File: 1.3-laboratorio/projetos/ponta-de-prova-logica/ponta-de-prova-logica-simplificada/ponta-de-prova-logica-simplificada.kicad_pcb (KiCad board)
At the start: 2 copper layers, 18 parts, among them J1 TEST PROBE, J2 Conn_01x02, U1 LM319

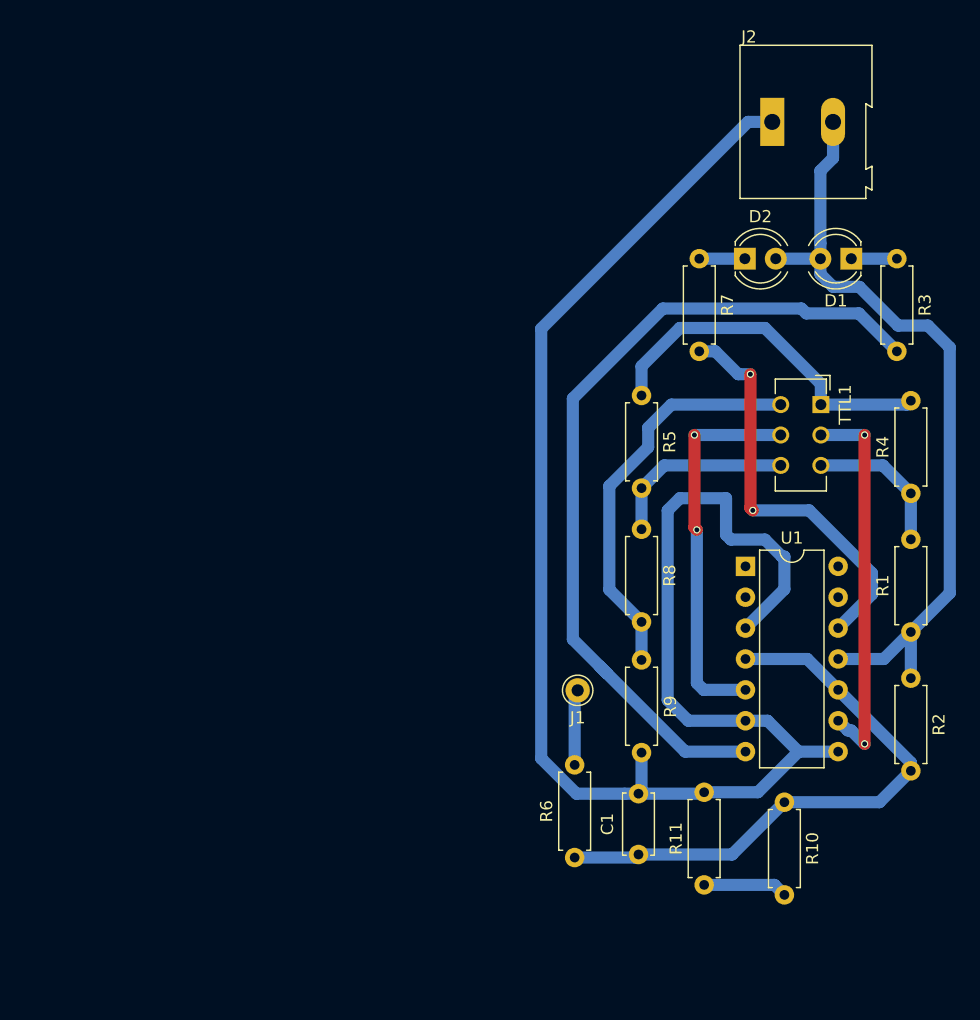
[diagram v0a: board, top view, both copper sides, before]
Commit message: Nova versão da Ponta de Prova Lógica - PCI em elaboração.
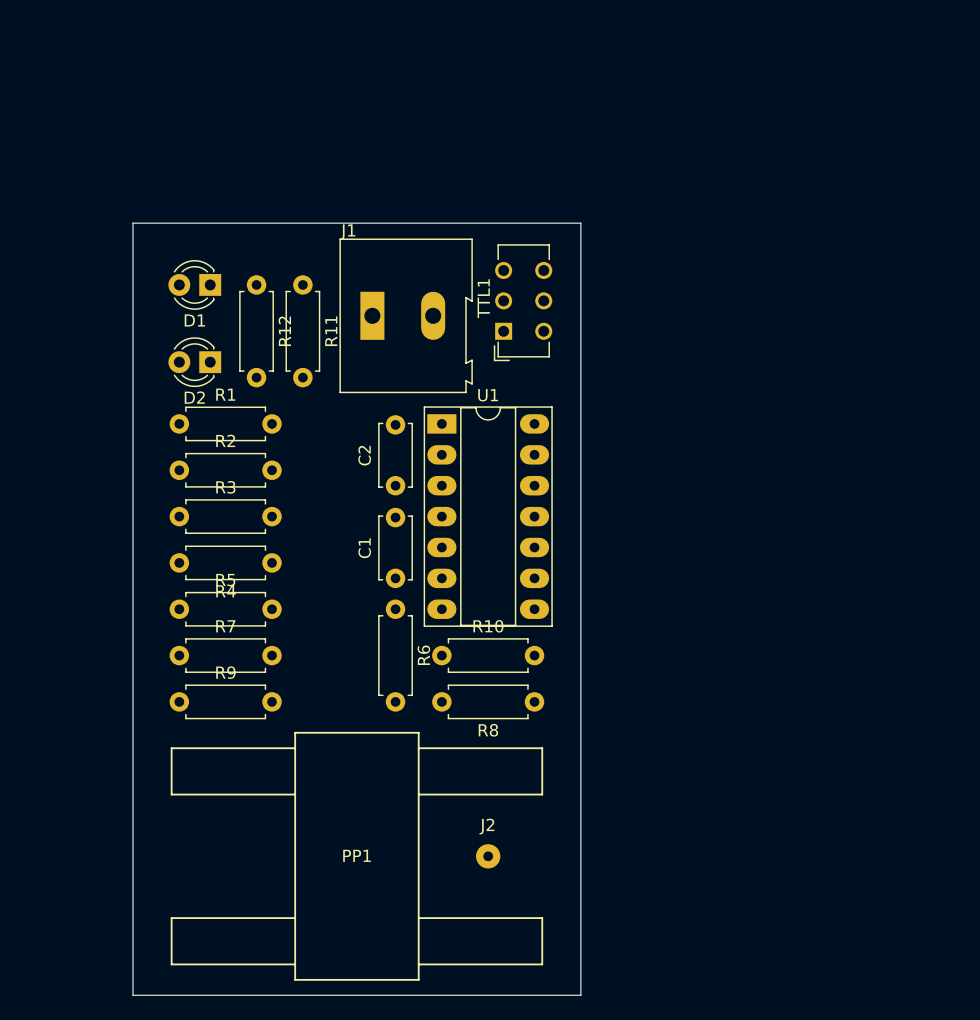
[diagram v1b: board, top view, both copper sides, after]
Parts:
- added C2: 100nF, Capacitor_THT:C_Disc_D5.0mm_W2.5mm_P5.00mm, F.Cu at (160.0, 90.2)
- added PP1: ponta-de-prova-fixacao-20mm-x-10mm-x-10mm, ponta-de-prova-fixacao-20mm-x-10mm-x-10mm, F.Cu at (151.8, 110.5)
- added R12: 820/0.5W, Resistor_THT:R_Axial_DIN0207_L6.3mm_D2.5mm_P7.62mm_Horizontal, F.Cu at (148.6, 73.7)
- C1: footprint Capacitors_THT:C_Disc_D5.0mm_W2.5mm_P5.00mm -> Capacitor_THT:C_Disc_D5.0mm_W2.5mm_P5.00mm
- D1: value LED HIGH -> LED ALTO; footprint LEDs:LED_D4.0mm -> LED_THT:LED_D3.0mm
- D2: value LED LOW -> LED BAIXO; footprint LEDs:LED_D4.0mm -> LED_THT:LED_D3.0mm
- J1: value TEST PROBE -> Conn_01x02; footprint Connectors:Pin_d1.0mm_L10.0mm -> TerminalBlock:TerminalBlock_Altech_AK300-2_P5.00mm
- J2: value Conn_01x02 -> PONTA DE PROVA; footprint Connectors_Terminal_Blocks:TerminalBlock_Altech_AK300-2_P5.00mm -> Connector_Wire:SolderWirePad_1x01_Drill0.8mm
- R1, R6: footprint Resistors_THT:R_Axial_DIN0207_L6.3mm_D2.5mm_P7.62mm_Horizontal -> Resistor_THT:R_Axial_DIN0207_L6.3mm_D2.5mm_P7.62mm_Horizontal
- R10: value 680k -> 10M; footprint Resistors_THT:R_Axial_DIN0207_L6.3mm_D2.5mm_P7.62mm_Horizontal -> Resistor_THT:R_Axial_DIN0207_L6.3mm_D2.5mm_P7.62mm_Horizontal
- R11: value 390k -> 820/0.5W; footprint Resistors_THT:R_Axial_DIN0207_L6.3mm_D2.5mm_P7.62mm_Horizontal -> Resistor_THT:R_Axial_DIN0207_L6.3mm_D2.5mm_P7.62mm_Horizontal
- R2: value 1.2M -> 56k; footprint Resistors_THT:R_Axial_DIN0207_L6.3mm_D2.5mm_P7.62mm_Horizontal -> Resistor_THT:R_Axial_DIN0207_L6.3mm_D2.5mm_P7.62mm_Horizontal
- R3: value 560/0.5W -> 22k; footprint Resistors_THT:R_Axial_DIN0207_L6.3mm_D2.5mm_P7.62mm_Horizontal -> Resistor_THT:R_Axial_DIN0207_L6.3mm_D2.5mm_P7.62mm_Horizontal
- R4: value 56k -> 47k; footprint Resistors_THT:R_Axial_DIN0207_L6.3mm_D2.5mm_P7.62mm_Horizontal -> Resistor_THT:R_Axial_DIN0207_L6.3mm_D2.5mm_P7.62mm_Horizontal
- R5: value 22k -> 33k; footprint Resistors_THT:R_Axial_DIN0207_L6.3mm_D2.5mm_P7.62mm_Horizontal -> Resistor_THT:R_Axial_DIN0207_L6.3mm_D2.5mm_P7.62mm_Horizontal
- R7: value 560/0.5W -> 1.2M; footprint Resistors_THT:R_Axial_DIN0207_L6.3mm_D2.5mm_P7.62mm_Horizontal -> Resistor_THT:R_Axial_DIN0207_L6.3mm_D2.5mm_P7.62mm_Horizontal
- R8: value 47k -> 680k; footprint Resistors_THT:R_Axial_DIN0207_L6.3mm_D2.5mm_P7.62mm_Horizontal -> Resistor_THT:R_Axial_DIN0207_L6.3mm_D2.5mm_P7.62mm_Horizontal
- R9: value 33k -> 390k; footprint Resistors_THT:R_Axial_DIN0207_L6.3mm_D2.5mm_P7.62mm_Horizontal -> Resistor_THT:R_Axial_DIN0207_L6.3mm_D2.5mm_P7.62mm_Horizontal
- TTL1: footprint Buttons_Switches_THT:SW_CuK_JS202011AQN_DPDT_Angled -> Button_Switch_THT:SW_CuK_JS202011CQN_DPDT_Straight
- U1: value LM319 -> LM339; footprint Housings_DIP:DIP-14_W7.62mm -> Package_DIP:DIP-14_W7.62mm_Socket_LongPads
- moved J2 64.8 mm to (167.6, 120.7)
- moved R3 62.7 mm to (142.2, 92.7), turned to 0 degrees
- moved R1 62.5 mm to (142.2, 85.1), turned to 0 degrees
- moved R2 62.5 mm to (142.2, 88.9), turned to 0 degrees
- moved R11 59.4 mm to (152.4, 73.7), turned to 270 degrees
- moved R7 53.8 mm to (142.2, 104.1), turned to 0 degrees
- moved R4 52.9 mm to (149.9, 96.5), turned to 180 degrees
- moved D1 52.8 mm to (144.8, 73.7)
- moved D2 44.8 mm to (144.8, 80.0), turned to 180 degrees
- moved R5 41.9 mm to (142.2, 100.3), turned to 0 degrees
- moved R9 38.2 mm to (142.2, 108.0), turned to 0 degrees
- moved J1 35.1 mm to (158.1, 76.2)
- moved R10 30.6 mm to (163.8, 104.1), turned to 0 degrees
- moved C1 30.2 mm to (160.0, 97.8)
- moved U1 27.6 mm to (163.8, 85.1)
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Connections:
- D1 pad 2: +5V -> VCC
- D2 pad 2: +5V -> VCC
- J1 pad 1: Net-(J1-Pad1) -> VCC
- J2 pad 1: GND -> Net-(J2-Pad1)
- R1 pad 1: +5V -> VCC
- R10 pad 1: Net-(C1-Pad1) -> Net-(R10-Pad1)
- R10 pad 2: Net-(R10-Pad2) -> GND
- R11 pad 1: Net-(R10-Pad2) -> Net-(D1-Pad1)
- R11 pad 2: GND -> Net-(R11-Pad2)
- R2 pad 1: +5V -> Net-(R1-Pad2)
- R2 pad 2: Net-(C1-Pad1) -> Net-(R2-Pad2)
- R3 pad 1: Net-(D1-Pad1) -> Net-(R2-Pad2)
- R4 pad 1: Net-(R1-Pad2) -> Net-(R3-Pad2)
- R5 pad 2: Net-(R5-Pad2) -> GND
- R6 pad 2: Net-(J1-Pad1) -> Net-(J2-Pad1)
- R7 pad 1: Net-(D2-Pad1) -> VCC
- R7 pad 2: Net-(R7-Pad2) -> Net-(C1-Pad1)
- R8 pad 1: Net-(R5-Pad2) -> Net-(C1-Pad1)
- TTL1 pad 1: Net-(R4-Pad2) -> Net-(R2-Pad2)
- TTL1 pad 4: Net-(R8-Pad2) -> Net-(R4-Pad2)
- TTL1 pad 5: Net-(TTL1-Pad5) -> Net-(R10-Pad1)
- TTL1 pad 6: Net-(R5-Pad2) -> Net-(R3-Pad2)
- U1 pad 1: Net-(U1-Pad1) -> Net-(R11-Pad2)
- U1 pad 10: Net-(C1-Pad1) -> GND
- U1 pad 11: +5V -> GND
- U1 pad 12: Net-(R7-Pad2) -> GND
- U1 pad 13: Net-(U1-Pad13) -> GND
- U1 pad 14: Net-(U1-Pad14) -> GND
- U1 pad 3: GND -> VCC
- U1 pad 4: Net-(C1-Pad1) -> Net-(R10-Pad1)
- U1 pad 5: Net-(TTL1-Pad5) -> Net-(C1-Pad1)
- U1 pad 6: GND -> Net-(C1-Pad1)
- U1 pad 7: Net-(R3-Pad2) -> Net-(TTL1-Pad2)
- U1 pad 9: Net-(TTL1-Pad2) -> GND
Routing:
- net GND: track 141.0 -> 0.00 mm
- net Net-(R3-Pad2): track 69.8 -> 0.00 mm
- net +5V: track 65.2 -> 0.00 mm
- net Net-(C1-Pad1): track 48.4 -> 0.00 mm
- net Net-(R7-Pad2): track 33.9 -> 0.00 mm, vias 2 -> 0
- net Net-(R8-Pad2): track 33.2 -> 0.00 mm
- net Net-(TTL1-Pad2): track 32.0 -> 0.00 mm, vias 2 -> 0
- net Net-(TTL1-Pad5): track 31.8 -> 0.00 mm, vias 2 -> 0
- net Net-(R4-Pad2): track 29.6 -> 0.00 mm
- net Net-(R5-Pad2): track 15.6 -> 0.00 mm
- net Net-(R1-Pad2): track 12.1 -> 0.00 mm
- net Net-(R10-Pad2): track 6.94 -> 0.00 mm
- net Net-(J1-Pad1): track 6.23 -> 0.00 mm
- net Net-(D2-Pad1): track 3.75 -> 0.00 mm
- net Net-(D1-Pad1): track 3.75 -> 0.00 mm
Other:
- board outline added: 36.8 x 63.5 mm
- net class Default: clearance 0.2 -> 0.25; trace_width 1 -> 0.5; via_dia 0.6 -> 2
- rule trace_clearance: 0.2 -> 0.25
- rule trace_min: 0.2 -> 0.5
- rule via_min_drill: 0.3 -> 0.4
- rule via_min_size: 0.4 -> 0.6

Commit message: Leiaute da PCB em andamento.
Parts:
- moved D1 41.9 mm to (134.6, 114.3), turned to 270 degrees
- moved R12 39.6 mm to (134.0, 110.5), turned to 0 degrees
- moved R11 36.7 mm to (134.0, 105.4), turned to 0 degrees
- moved D2 34.5 mm to (141.0, 114.3), turned to 270 degrees
- moved J1 31.1 mm to (137.8, 99.7), turned to 90 degrees
- moved TTL1 30.8 mm to (140.3, 88.9), turned to 180 degrees
- moved R9 29.5 mm to (171.4, 111.8), turned to 180 degrees
- moved U1 28.1 mm to (154.9, 111.8), turned to 180 degrees
- moved R7 25.0 mm to (163.8, 116.8)
- moved R5 23.3 mm to (163.8, 91.4)
- moved R2 22.9 mm to (163.8, 96.5)
- moved PP1 21.4 mm to (172.7, 106.0), turned to 90 degrees
- moved C2 20.4 mm to (158.8, 110.5)
- moved J2 17.6 mm to (182.9, 111.8), turned to 90 degrees
- moved R4 17.3 mm to (163.8, 86.4), turned to 0 degrees
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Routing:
- net VCC: track 0.00 -> 81.7 mm
- net Net-(R11-Pad2): track 0.00 -> 29.0 mm, vias 0 -> 2
- net Net-(R10-Pad1): track 0.00 -> 20.9 mm, vias 0 -> 2
- net Net-(D1-Pad1): track 0.00 -> 11.4 mm
- net Net-(D2-Pad1): track 0.00 -> 9.30 mm
- net Net-(R12-Pad2): track 0.00 -> 4.97 mm
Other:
- board size 36.8 x 63.5 mm -> 63.5 x 36.8 mm
- net class Default: trace_width 0.5 -> 0.25
- net class Vcc added: clearance 0.25, trace_width 0.5, via_dia 2, via_drill 0.4
- rule trace_min: 0.5 -> 0.25

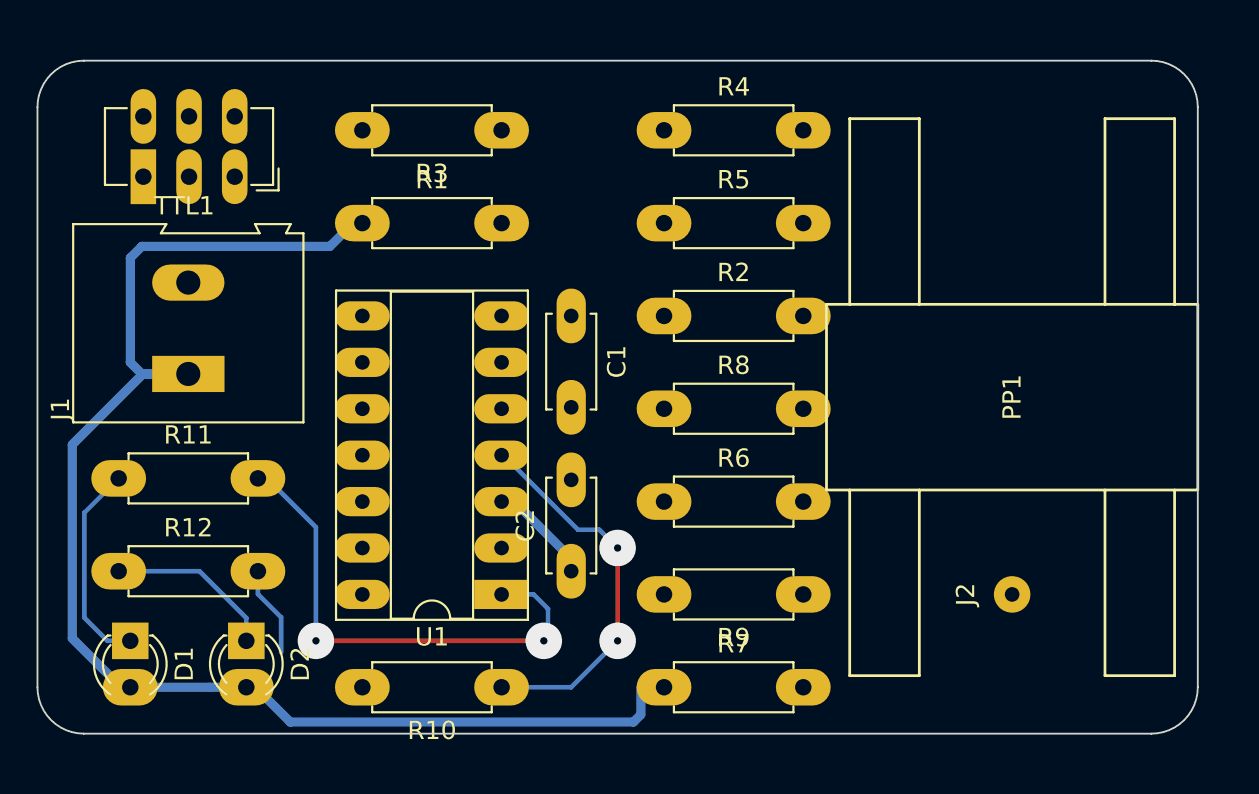
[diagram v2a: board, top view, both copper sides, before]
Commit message: Leiaute da placa da Ponta de Prova Lógica concluído. Falta ajustar F.SilkS.
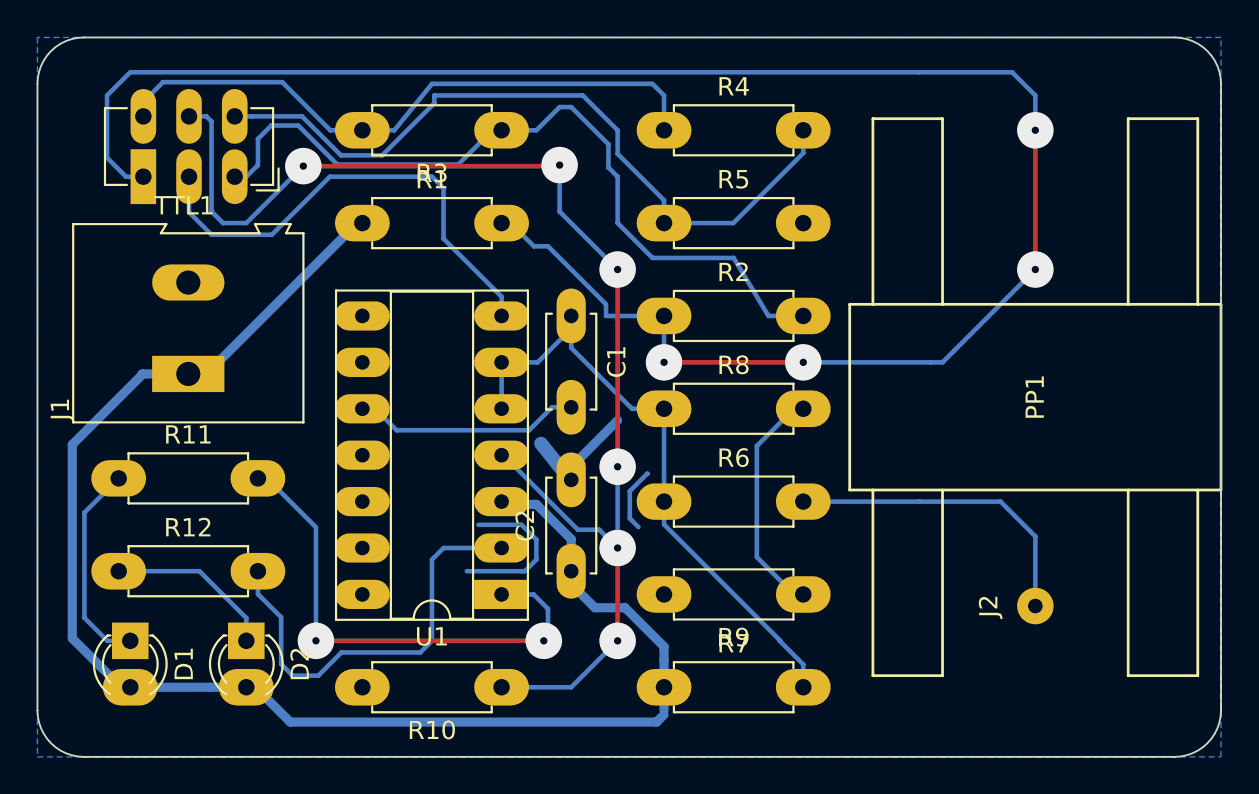
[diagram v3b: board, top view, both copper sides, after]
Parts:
- moved J2 1.42 mm to (184.2, 112.4)
- moved PP1 1.27 mm to (174.0, 106.0)
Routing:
- net Net-(R1-Pad2): track 0.00 -> 103.5 mm, vias 0 -> 4
- net Net-(R10-Pad1): track 20.9 -> 70.8 mm, vias 2 -> 6
- net Net-(R2-Pad2): track 0.00 -> 43.3 mm
- net Net-(R4-Pad2): track 0.00 -> 41.3 mm
- net Net-(C1-Pad1): track 0.00 -> 34.9 mm
- net Net-(R3-Pad2): track 0.00 -> 34.2 mm
- net GND: track 0.00 -> 32.1 mm
- net Net-(TTL1-Pad2): track 0.00 -> 26.3 mm
- net Net-(R12-Pad2): track 4.97 -> 23.4 mm
- net Net-(J2-Pad1): track 0.00 -> 17.3 mm
- net Net-(R8-Pad2): track 0.00 -> 12.8 mm
- net VCC: track 81.7 -> 83.1 mm
- added copper zone on B.Cu, net GND
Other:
- board size 63.5 x 36.8 mm -> 64.8 x 39.4 mm

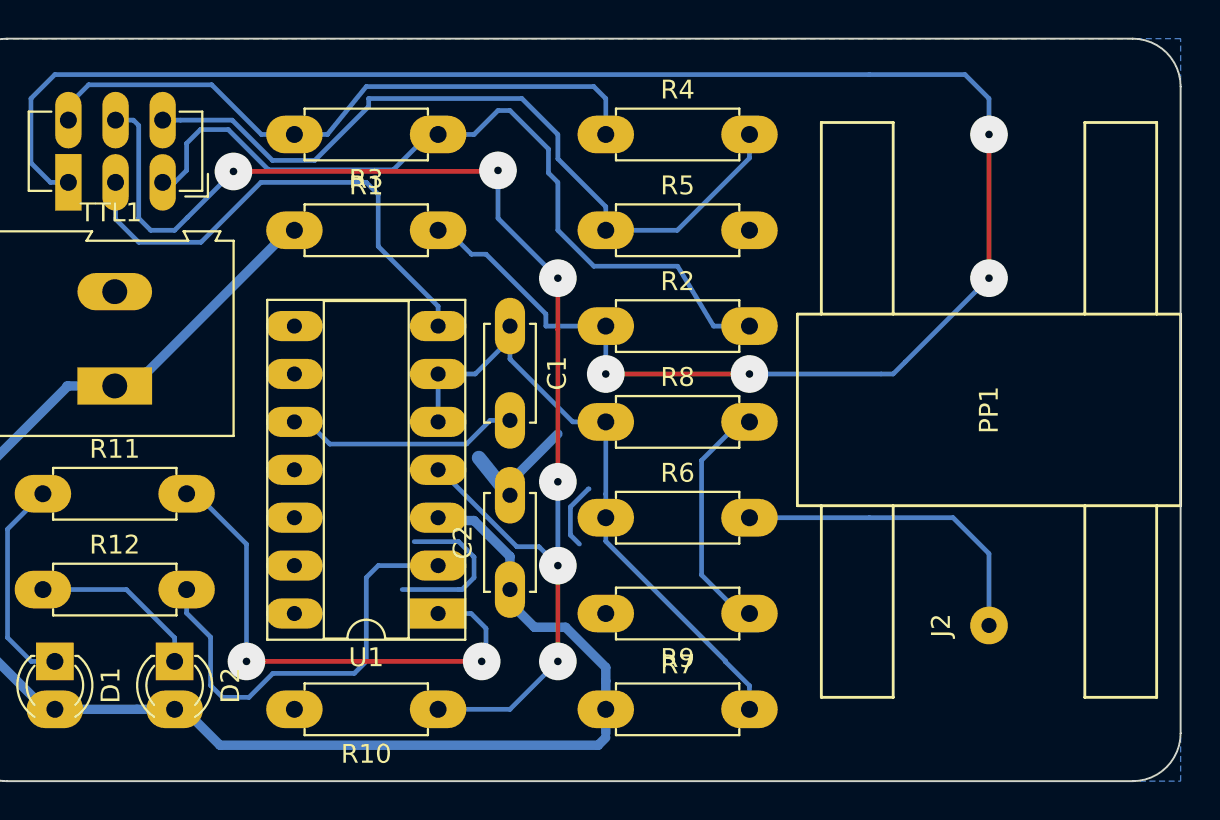
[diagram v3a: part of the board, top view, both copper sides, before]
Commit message: Ajustes no leiaute do PCB. Falta puxar os resistores próximos à chave.
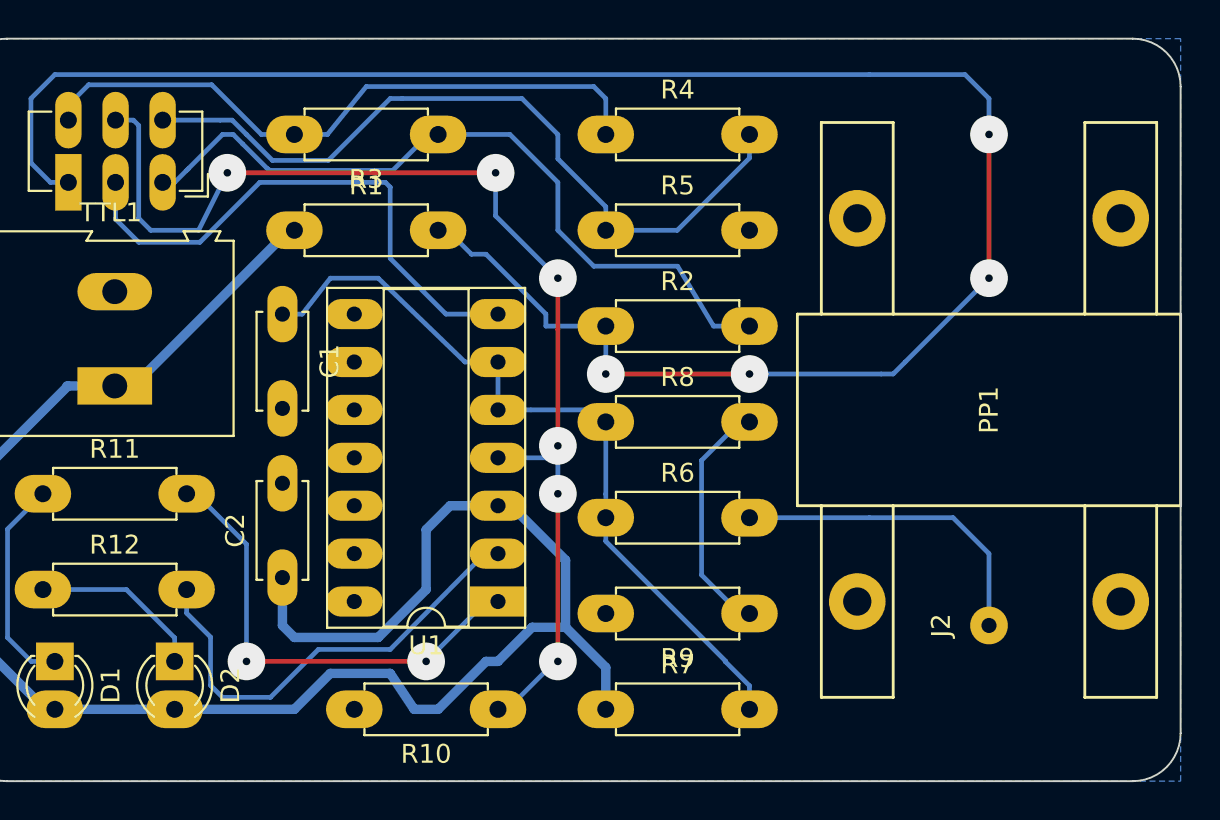
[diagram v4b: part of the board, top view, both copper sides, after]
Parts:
- moved C1 12.1 mm to (146.7, 95.9)
- moved C2 12.1 mm to (146.7, 109.9)
- moved U1 3.24 mm to (158.1, 111.1)
- moved R10 3.18 mm to (158.1, 116.8)
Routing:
- net GND: track 32.1 -> 0.00 mm
- net VCC: track 83.1 -> 100.1 mm
- net Net-(R10-Pad1): track 70.8 -> 62.9 mm
- net Net-(C1-Pad1): track 34.9 -> 41.6 mm
- net Net-(R11-Pad2): track 29.0 -> 25.1 mm
- net Net-(TTL1-Pad2): track 26.3 -> 29.2 mm
- net Net-(R2-Pad2): track 43.3 -> 40.7 mm
- net Net-(R12-Pad2): track 23.4 -> 24.3 mm
